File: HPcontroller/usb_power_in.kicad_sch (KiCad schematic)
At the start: 12 parts, among them J2 USB_C_Receptacle, Q2 AON7410

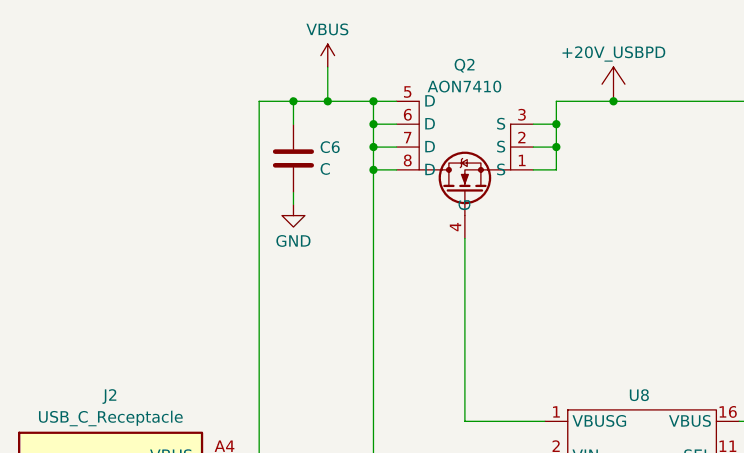
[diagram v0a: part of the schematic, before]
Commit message: design "finished" need to do bom and footprints and layout
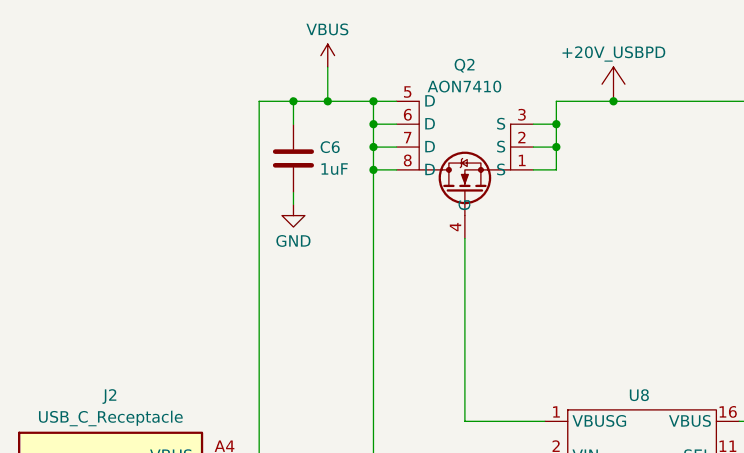
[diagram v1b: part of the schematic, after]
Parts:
- C6: value C -> 1uF; footprint (none) -> Capacitor_SMD:C_0805_2012Metric_Pad1.18x1.45mm_HandSolder
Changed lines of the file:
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@@
       (effects (font (size 1.27 1.27)) (justify left))
     )
-    (property "Value" "C" (at 71.501 34.2321 0)
+    (property "Value" "1uF" (at 71.501 34.2321 0)
       (effects (font (size 1.27 1.27)) (justify left))
     )
-    (property "Footprint" "" (at 69.5452 36.83 0)
+    (property "Footprint" "Capacitor_SMD:C_0805_2012Metric_Pad1.18x1.45mm_HandSolder" (at 69.5452 36.83 0)
       (effects (font (size 1.27 1.27)) hide)
     )

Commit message: started routing, finished footprintns
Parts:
- removed R16, R17, R18: R, symbol Device:R
- added C14: 10uF, Capacitor_SMD:C_0805_2012Metric, symbol Device:C
- added R1, R4: 5.1k, Resistor_SMD:R_0603_1608Metric, symbol Device:R
- added R5: 100k, Resistor_SMD:R_0603_1608Metric, symbol Device:R
- C6: footprint Capacitor_SMD:C_0805_2012Metric_Pad1.18x1.45mm_HandSolder -> Capacitor_SMD:C_0603_1608Metric; MPN (none) -> UMK107BJ105KA-T; Voltage (none) -> 25V
- J2: footprint (none) -> Connector_USB:USB_C_Receptacle_JAE_DX07S016JA1R1500; MPN (none) -> DX07S016JA1R1500
- MOD1: footprint PD_HV_footprints:MORNSUN_K7803JT-500R3-LB -> HPfootprint:MORNSUN_K7803JT-500R3-LB
- Q2: footprint (none) -> HPfootprint:DFN3X3A_8L_EPA1_P_AOS; MPN (none) -> AON7410
- U8: value ~ -> IP2721; footprint (none) -> Package_SO:TSSOP-16_4.4x5mm_P0.65mm
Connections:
- net +20V_USBPD: now also C14.1
- net CC1: now also R1.1
- net CC2: now also R4.1
- net GND: now also C14.2, R1.2, R4.2
- net VBUS: now also R5.1
- net at U8.11 (SEL): now also R5.2

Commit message: finished routing, moving on to heater
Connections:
- net CC1: now also D2.3 (TVS2); no longer D2.1 (TVS1)
- net CC2: now also D2.1 (TVS1); no longer D2.3 (TVS2)
- net +3.3V renamed +3V3
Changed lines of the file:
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@@
     (effects (font (size 1.27 1.27)) (justify left bottom))
   )
-  (label "CC2" (at 88.9 106.68 0) (fields_autoplaced)
+  (label "CC2" (at 88.9 104.14 0) (fields_autoplaced)
     (effects (font (size 1.27 1.27)) (justify left bottom))
   )
-  (label "CC1" (at 88.9 104.14 0) (fields_autoplaced)
+  (label "CC1" (at 88.9 106.68 0) (fields_autoplaced)
     (effects (font (size 1.27 1.27)) (justify left bottom))
   )
@@
     )
   )
+  (symbol (lib_id "power:+3V3") (at 214.63 55.88 0) (unit 1)
+    (in_bom yes) (on_board yes) (dnp no) (fields_autoplaced)
+    (property "Reference" "#PWR027" (at 214.63 59.69 0)
+      (effects (font (size 1.27 1.27)) hide)
+    )
+    (property "Value" "+3V3" (at 214.63 50.8 0)
+      (effects (font (size 1.27 1.27)))
+    )
+    (property "Footprint" "" (at 214.63 55.88 0)
+      (effects (font (size 1.27 1.27)) hide)
+    )
+    (property "Datasheet" "" (at 214.63 55.88 0)
+      (effects (font (size 1.27 1.27)) hide)
+    )
+    (pin "1")
+    (instances
+      (project "HPcontroller"
+        (path "/e63e39d7-6ac0-4ffd-8aa3-1841a4541b55/2576b983-b407-4bb3-870d-6fa0fab97bf4"
+          (reference "#PWR027") (unit 1)
+        )
+        (path "/e63e39d7-6ac0-4ffd-8aa3-1841a4541b55/0b8713ad-7947-4b4a-b845-8beba6d3af66"
+          (reference "#PWR016") (unit 1)
+        )
+      )
+    )
+  )
   (symbol (lib_id "Device:C") (at 68.58 33.02 0) (unit 1)
     (in_bom yes) (on_board yes) (dnp no) (fields_autoplaced)
@@
         )
       )
-    )
-  )
-  (symbol (lib_id "power:+3.3V") (at 214.63 55.88 0) (unit 1)
-    (in_bom yes) (on_board yes) (dnp no) (fields_autoplaced)
-    (property "Reference" "#PWR012" (at 214.63 59.69 0)
-      (effects (font (size 1.27 1.27)) hide)
-    )
-    (property "Value" "+3.3V" (at 214.63 50.8 0)
-      (effects (font (size 1.27 1.27)))
-    )
-    (property "Footprint" "" (at 214.63 55.88 0)
-      (effects (font (size 1.27 1.27)) hide)
-    )
-    (property "Datasheet" "" (at 214.63 55.88 0)
-      (effects (font (size 1.27 1.27)) hide)
-    )
-    (pin "1")
-    (instances
-      (project "HPcontroller"
-        (path "/e63e39d7-6ac0-4ffd-8aa3-1841a4541b55/0b8713ad-7947-4b4a-b845-8beba6d3af66"
-          (reference "#PWR012") (unit 1)
-        )
-      )

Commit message: worked on bom, orderables from dk are in
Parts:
- C14, C7: Digikey PN (none) -> 490-18663-1-ND
- C6: Digikey PN (none) -> 587-2400-1-ND
- C8: Digikey PN (none) -> CL10A226MP8NUNE
- D2: Digikey PN (none) -> 497-6635-1-ND; MPN (none) -> ESDA6V1BC6
- J2: Digikey PN (none) -> 670-DX07S016JA1R1500CT-ND
- MOD1: Digikey PN (none) -> 2725-K7803JT-500R3-LBCT-ND
- Q2: Digikey PN (none) -> 785-1581-1-ND
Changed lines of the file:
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@@
+      (effects (font (size 1.27 1.27)) hide)
+    )
+    (property "Digikey PN" "785-1581-1-ND" (at 87.63 35.56 0)
       (effects (font (size 1.27 1.27)) hide)
     )
@@
       (effects (font (size 1.27 1.27)) hide)
     )
+    (property "Digikey PN" "490-18663-1-ND" (at 110.49 30.48 0)
+      (effects (font (size 1.27 1.27)) hide)
+    )
     (pin "1")
     (pin "2")
@@
     )
     (property "Datasheet" "http://www.st.com/content/ccc/resource/technical/document/datasheet/21/07/21/e3/a8/df/42/a2/CD00001906.pdf/files/CD00001906.pdf/jcr:content/translations/en.CD00001906.pdf" (at 88.9 121.92 90)
+      (effects (font (size 1.27 1.27)) hide)
+    )
+    (property "Digikey PN" "497-6635-1-ND" (at 88.9 121.92 0)
+      (effects (font (size 1.27 1.27)) hide)
+    )
+    (property "MPN" "ESDA6V1BC6" (at 88.9 121.92 0)
       (effects (font (size 1.27 1.27)) hide)
     )
@@
       (effects (font (size 1.27 1.27)) hide)
     )
+    (property "Digikey PN" "490-18663-1-ND" (at 177.8 66.675 0)
+      (effects (font (size 1.27 1.27)) hide)
+    )
     (pin "1")
     (pin "2")
@@
     )
     (property "MPN" "K7803JT-500R3-LB" (at 194.945 61.595 0)
+      (effects (font (size 1.27 1.27)) hide)
+    )
+    (property "Digikey PN" "2725-K7803JT-500R3-LBCT-ND" (at 194.945 61.595 0)
       (effects (font (size 1.27 1.27)) hide)
     )
@@
     )
     (property "MPN" "DX07S016JA1R1500" (at 48.26 91.44 0)
+      (effects (font (size 1.27 1.27)) hide)
+    )
+    (property "Digikey PN" "670-DX07S016JA1R1500CT-ND" (at 48.26 91.44 0)
       (effects (font (size 1.27 1.27)) hide)
     )
@@
       (effects (font (size 1.27 1.27)) hide)
     )
+    (property "Digikey PN" "587-2400-1-ND" (at 68.58 33.02 0)
+      (effects (font (size 1.27 1.27)) hide)
+    )
     (pin "1")
     (pin "2")
@@
       (effects (font (size 1.27 1.27)) hide)
     )
+    (property "Digikey PN" "CL10A226MP8NUNE" (at 214.63 66.675 0)
+      (effects (font (size 1.27 1.27)) hide)
+    )

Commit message: v3 routing
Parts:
- removed D2: ESDA6V1BC6, Package_TO_SOT_SMD:SOT-23-6, symbol Power_Protection:ESDA6V1BC6
- removed J2: USB_C_Receptacle, Connector_USB:USB_C_Receptacle_JAE_DX07S016JA1R1500, symbol Connector:USB_C_Receptacle
- removed MOD1: K7803JT-500R3-LB, HPfootprint:MORNSUN_K7803JT-500R3-LB, symbol PDHV_sym:K7803JT-500R3-LB
- removed Q2: AON7410, HPfootprint:DFN3X3A_8L_EPA1_P_AOS, symbol PDHV_sym:AON7410
- removed U8: IP2721, Package_SO:TSSOP-16_4.4x5mm_P0.65mm, symbol project_assorted:IP2721
- added C15: 10uF 50V, Capacitor_SMD:C_1206_3216Metric_Pad1.33x1.80mm_HandSolder, symbol Device:C
- added D1: LED, LED_SMD:LED_0603_1608Metric_Pad1.05x0.95mm_HandSolder, symbol Device:LED
- added J2: UJ20-C-H-G-SMT-1-P16-TR, hotplate_Library:SAMESKY_UJ20-C-H-G-SMT-1-P16-TR, symbol mpssym:UJ20-C-H-G-SMT-1-P16-TR
- added Q2: ~, hotplate_Library:LFPAK56D, symbol Hotplate_Library:BUK9K25-40RAX
- added R11: 100, Resistor_SMD:R_0402_1005Metric_Pad0.72x0.64mm_HandSolder, symbol Device:R
- added R14, R15: 10, Resistor_SMD:R_0402_1005Metric_Pad0.72x0.64mm_HandSolder, symbol Device:R
- added R16, R17: 5k1 1%, Resistor_SMD:R_0402_1005Metric_Pad0.72x0.64mm_HandSolder, symbol Device:R
- added R6: 26k, Resistor_SMD:R_0603_1608Metric_Pad0.98x0.95mm_HandSolder, symbol Device:R
- added TP1, TP2, TP3, TP8: TestPoint, TestPoint:TestPoint_Pad_D1.5mm, symbol Connector:TestPoint
- added U5: AP33771C, Package_DFN_QFN:DFN-14-1EP_3x3mm_P0.4mm_EP1.78x2.35mm, symbol C_buck_syms:AP33771C
- added U8: ~, hotplate_Library:D78B33-0.5, symbol Hotplate_Library:D78B33-0.5
- C14: value 10uF -> 1uF 25V; footprint Capacitor_SMD:C_0805_2012Metric -> Capacitor_SMD:C_0402_1005Metric_Pad0.74x0.62mm_HandSolder; Digikey PN 490-18663-1-ND -> (none); MPN GRM21BR61H106KE43L -> 0402X105K250CT; Voltage 50V -> (none)
- C6: value 1uF -> 10uF 50V; footprint Capacitor_SMD:C_0603_1608Metric -> Capacitor_SMD:C_1206_3216Metric_Pad1.33x1.80mm_HandSolder; Digikey PN 587-2400-1-ND -> (none); MPN UMK107BJ105KA-T -> CL31A106KBHNNNE; Voltage 25V -> (none)
- R1: value 5.1k -> 5k1 1%; footprint Resistor_SMD:R_0603_1608Metric -> Resistor_SMD:R_0402_1005Metric_Pad0.72x0.64mm_HandSolder; Digikey PN RMCF0603FT5K10CT-ND -> (none); MPN RMCF0603FT5K10 -> RC0402FR-135K1L; Tol 1% -> (none)
- R4: value 5.1k -> 1k; footprint Resistor_SMD:R_0603_1608Metric -> Resistor_SMD:R_0402_1005Metric_Pad0.72x0.64mm_HandSolder; Digikey PN RMCF0603FT5K10CT-ND -> (none); MPN RMCF0603FT5K10 -> RC0402FR-071KL; Tol 1% -> (none)
- R5: value 100k -> 5m; footprint Resistor_SMD:R_0603_1608Metric -> Resistor_SMD:R_0603_1608Metric_Pad0.98x0.95mm_HandSolder; Digikey PN RMCF0603JG100KCT-ND -> (none); MPN RMCF0603JG100K -> PA0603FRE470R005L
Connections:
- net +3V3: now also U8.3 (3v3_Out)
- net CC1: now also J2.A5 (CC1), R16.1, U5.11 (CC1); no longer R1.1
- net CC2: now also R1.1, J2.B5 (CC2), U5.10 (CC2); no longer R4.1
- net GND: now also C15.2, D1.1 (K), J2.A1_B12 (GND), J2.B1_A12 (GND__1), J2.SH1 (SHIELD), J2.SH2 (SHIELD__1), J2.SH3 (SHIELD__2), J2.SH4 (SHIELD__3), R16.2, R17.2, R6.2, U5.15 (EPAD/GND), U5.5 (Gnd), U8.2 (Gnd); no longer R4.2
- net at R5.2: now also Q2.5 (D2), TP2.1, U5.3 (Vcc)
- net +20V_USBPD: no longer names the net of C14.1
- net +20V_USBPD: now also U5.14 (V5V); no longer C7.1
- net VBUS renamed VUSB_RAW
- net VUSB_RAW: now also J2.A4_B9 (VBUS), J2.B4_A9 (VBUS__1), TP1.1, U5.4 (ISenP)
- new net: R11.2, U5.1 (Vout)
- new net: R4.1, U5.7 (LED)
- new net: D1.2 (A), R4.2
- new net: R14.2, R15.2, TP3.1, U5.2 (PWR_EN)
- new net: R6.1, U5.8 (VSel)
- new net: R17.1, U5.9 (ISel)
- new net: Q2.4 (G2), R14.1
- new net: Q2.1 (S1), Q2.3 (S2), TP8.1
- new net: Q2.2 (G1), R15.1
- new net +28V: C15.1, C7.1, Q2.7 (D1), R11.1, U8.1 (Vin)
- new net DN: J2.A7 (DN1), J2.B7 (DN2), U5.12 (DN)
- new net DP: J2.A6 (DP1), J2.B6 (DP2), U5.13 (DP)
- new net FLIP: U5.6 (FLIP)
- no-connect marks 16 -> 2
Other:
- note added: "Requests 5A 12V"
- note removed: "SEL VTG HIGH 20V LOW 5V FLOAT 15V"
- moved on the sheet: C7, C8, TP_3V1

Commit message: finished temp meas stuff, laying out
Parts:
- C14: footprint Capacitor_SMD:C_0402_1005Metric_Pad0.74x0.62mm_HandSolder -> Capacitor_SMD:C_0402_1005Metric
- J2: MPN (none) -> UJ20-C-H-G-SMT-1-P16-TR
- Q2: MPN (none) -> BUK9K25-40RAX
- R1, R11, R14, R15, R16, R17, R4: footprint Resistor_SMD:R_0402_1005Metric_Pad0.72x0.64mm_HandSolder -> Resistor_SMD:R_0402_1005Metric
- R5: footprint Resistor_SMD:R_0603_1608Metric_Pad0.98x0.95mm_HandSolder -> Resistor_SMD:R_0603_1608Metric
- R6: footprint Resistor_SMD:R_0603_1608Metric_Pad0.98x0.95mm_HandSolder -> Resistor_SMD:R_0603_1608Metric; MPN (none) -> RC0603FR-0726K1L; Tol (none) -> 1%
- TP_3V1: footprint TestPoint:TestPoint_Pad_D1.0mm -> TestPoint:TestPoint_Pad_D1.5mm
- U8: MPN (none) -> D78B33-0.5
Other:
- note added: "Requests 5A 28V"
- note removed: "Requests 5A 12V"
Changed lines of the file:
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@@
 	(generator_version "9.0")
 	(paper "A4")
-	(text "Requests\n5A 12V"
+	(text "Requests\n5A 28V"
 		(exclude_from_sim no)
 		(at 129.54 130.302 0)
@@
 			)
 		)
-		(property "Footprint" "Resistor_SMD:R_0402_1005Metric_Pad0.72x0.64mm_HandSolder"
+		(property "Footprint" "Resistor_SMD:R_0402_1005Metric"
 			(at 70.612 116.84 90)
 			(effects
@@
 			)
 		)
-		(property "Footprint" "Resistor_SMD:R_0402_1005Metric_Pad0.72x0.64mm_HandSolder"
+		(property "Footprint" "Resistor_SMD:R_0402_1005Metric"
 			(at 135.382 77.47 90)
 			(effects
@@
 			)
 		)
-		(property "Footprint" "TestPoint:TestPoint_Pad_D1.0mm"
+		(property "Footprint" "TestPoint:TestPoint_Pad_D1.5mm"
 			(at 264.16 38.1 0)
 			(effects
@@
 			)
 		)
-		(property "Footprint" "Resistor_SMD:R_0402_1005Metric_Pad0.72x0.64mm_HandSolder"
+		(property "Footprint" "Resistor_SMD:R_0402_1005Metric"
 			(at 84.582 123.19 90)
 			(effects
@@
 			)
 		)
+		(property "MPN" "D78B33-0.5"
+			(at 234.95 46.99 0)
+			(effects
+				(font
+					(size 1.27 1.27)
+				)
+				(hide yes)
+			)
+		)
 		(pin "2"
 		)
@@
 			)
 		)
-		(property "Footprint" "Resistor_SMD:R_0402_1005Metric_Pad0.72x0.64mm_HandSolder"
+		(property "Footprint" "Resistor_SMD:R_0402_1005Metric"
 			(at 132.842 119.38 90)
 			(effects
@@
 			)
 		)
-		(property "Footprint" "Resistor_SMD:R_0402_1005Metric_Pad0.72x0.64mm_HandSolder"
+		(property "Footprint" "Resistor_SMD:R_0402_1005Metric"
 			(at 107.442 76.2 90)
 			(effects
@@
 			)
 		)
+		(property "MPN" "BUK9K25-40RAX"
+			(at 120.65 27.94 90)
+			(effects
+				(font
+					(size 1.27 1.27)
+				)
+				(hide yes)
+			)
+		)
 		(pin "4"
 		)
@@
 			)
 		)
-		(property "Footprint" "Resistor_SMD:R_0603_1608Metric_Pad0.98x0.95mm_HandSolder"
+		(property "Footprint" "Resistor_SMD:R_0603_1608Metric"
 			(at 83.82 66.548 90)
 			(effects
@@
 			)
 		)
-		(property "Footprint" "Resistor_SMD:R_0402_1005Metric_Pad0.72x0.64mm_HandSolder"
+		(property "Footprint" "Resistor_SMD:R_0402_1005Metric"
 			(at 125.222 76.2 90)
 			(effects
@@
 			)
 		)
-		(property "Footprint" "Resistor_SMD:R_0603_1608Metric_Pad0.98x0.95mm_HandSolder"
+		(property "Footprint" "Resistor_SMD:R_0603_1608Metric"
 			(at 121.412 119.38 90)
 			(effects
@@
 			)
 		)
-		(property "MPN" ""
+		(property "MPN" "RC0603FR-0726K1L"
 			(at 123.19 119.38 0)
 			(effects
@@
 			)
 		)
-		(property "Tol" ""
+		(property "Tol" "1%"
 			(at 123.19 119.38 0)
 			(effects
@@
 			)
 		)
-		(property "Footprint" "Capacitor_SMD:C_0402_1005Metric_Pad0.74x0.62mm_HandSolder"
+		(property "Footprint" "Capacitor_SMD:C_0402_1005Metric"
 			(at 145.7452 101.6 0)
 			(effects
@@
 			)
 		)
+		(property "MPN" "UJ20-C-H-G-SMT-1-P16-TR"
+			(at 29.21 85.09 0)
+			(effects
+				(font
+					(size 1.27 1.27)
+				)
+				(hide yes)
+			)
+		)
 		(pin "B4_A9"
 		)
@@
 			)
 		)
-		(property "Footprint" "Resistor_SMD:R_0402_1005Metric_Pad0.72x0.64mm_HandSolder"
+		(property "Footprint" "Resistor_SMD:R_0402_1005Metric"
 			(at 64.262 111.76 90)
 			(effects
